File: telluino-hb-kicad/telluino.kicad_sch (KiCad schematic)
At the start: 78 parts, among them J1 6P2C, J2 USB_A, Q1 MMBT3904, Q2 ZXTP2012Z, U1 LE9641PQC, U2 TISP61089BDR-S, U3 CH340C, U4 TXS0108EPWRG4

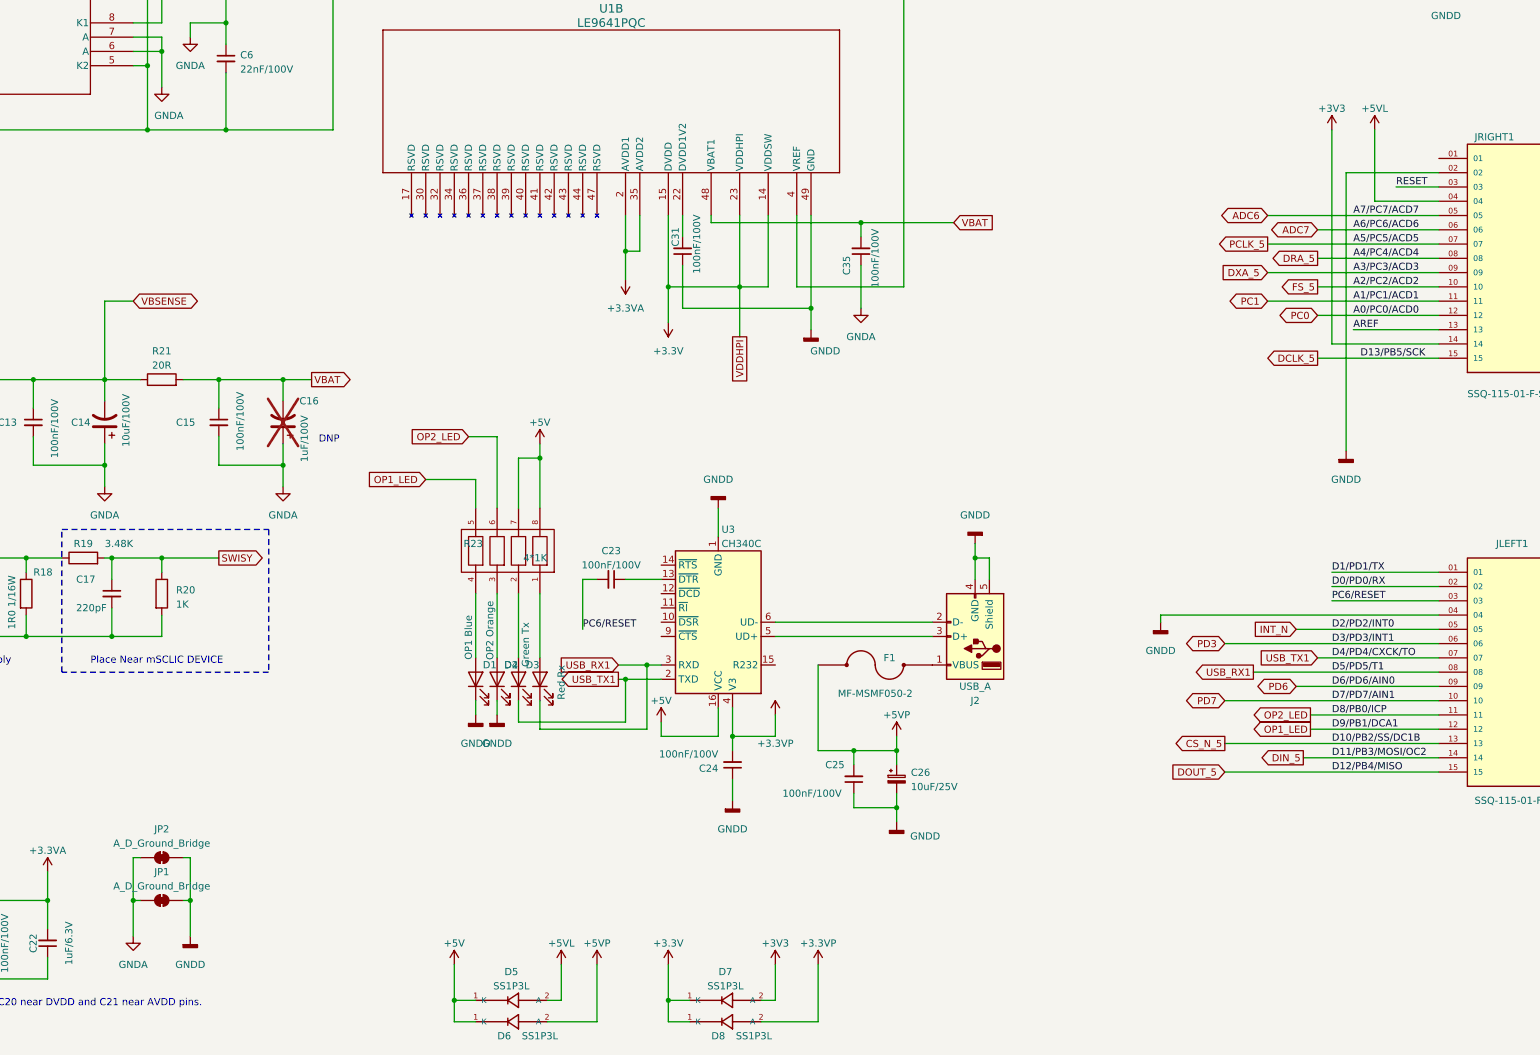
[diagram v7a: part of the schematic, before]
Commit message: rework 3.3 power supply
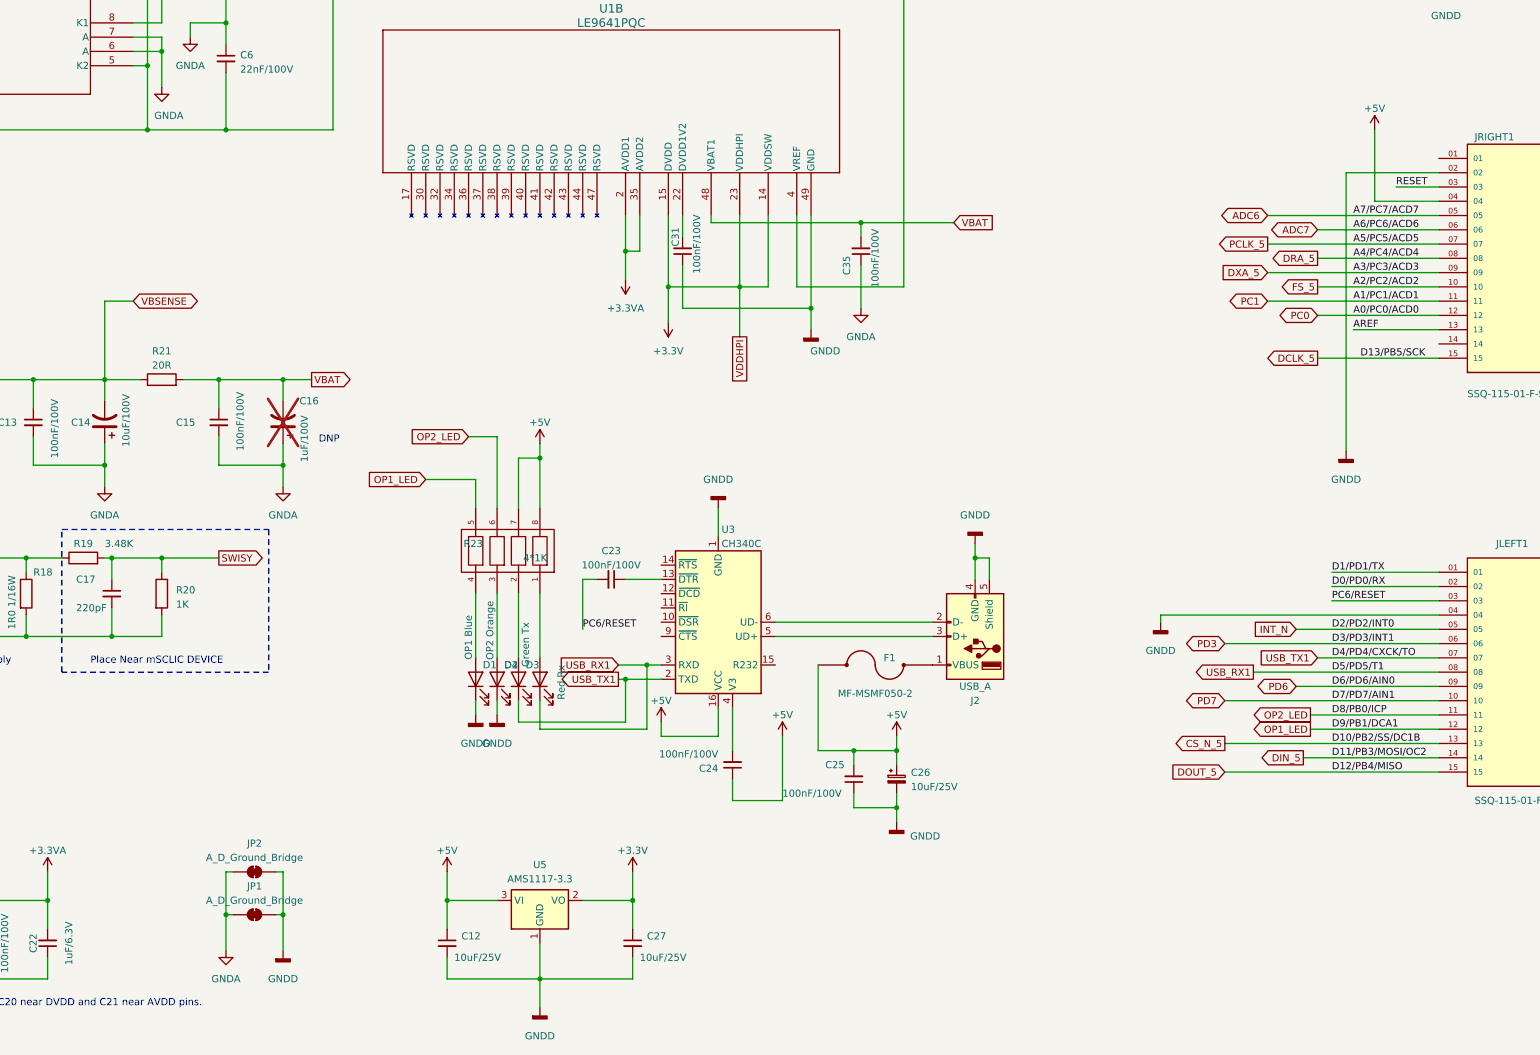
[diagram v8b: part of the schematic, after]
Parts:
- removed D5, D6, D7, D8: SS1P3L, my_lib:DO220AAL, symbol SS1P3L:SS1P3L
- added C12, C27: 10uF/25V, Capacitor_SMD:C_0603_1608Metric, symbol Device:C_Small
- added U5: AMS1117-3.3, Package_TO_SOT_SMD:SOT-223-3_TabPin2, symbol Regulator_Linear:AMS1117-3.3
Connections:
- net +5VL is gone; now on net +5V: JRIGHT1.04
- net +5VP is gone; now on net +5V: C25.2, C26.1, F1.2
- net +3.3V: now also C27.1, U5.2 (VO)
- net +5V: now also C24.1, C12.1, U5.3 (VI)
- net GNDD: now also C12.2, C27.2, U5.1 (GND); no longer C24.1
- net +3.3VP: no longer names the net of C24.2, U3.4 (V3)
- net +3V3: no longer names the net of JRIGHT1.14
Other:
- moved on the sheet: JP1, JP2
